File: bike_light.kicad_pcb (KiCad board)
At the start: 4 copper layers, 139.3 x 22.9 mm, 191 parts, among them P1 CONN_6_RA_MALE, P10 CONN_2, P11 CONN_2, P12 CONN_2, P13 CONN_2, P14 CONN_2, P15 CONN_2, P16 CONN_2, P2 CONN_2x2_MALE_RA, P3 CONN_2x2_MALE_RA, P4 CONN_2x2_FEMALE_BACK, P5 CONN_6_FEMALE_FRONT, P6 CONN_2x2_FEMALE_BACK, P7 CONN_2, P8 CONN_2, P9 CONN_2, Q1 AON7611, Q4 DMN65D8L, Q5 DMN65D8L, Q6 DMN65D8L, Q7 DMN65D8L, Q8 DMN65D8L, Q9 DMN65D8L, U1 TEST_PT, U10 TEST_PT, U11 TEST_PT, U12 TEST_PT, U13 TEST_PT, U14 TEST_PT, U15 TEST_PT, U16 TEST_PT, U17 TEST_PT, U18 TEST_PT, U19 TEST_PT, U2 TEST_PT, U20 MCP6L02, U21 74LVC2G06, U22 TPS3700, U23 NC7WZ08, U3 TEST_PT, U30 MSP430G2203IPW28, U31 BH1620FVC, U32 MMA7660FC, U33 AT42QT1011, U34 TOUCHPAD, U35 AT42QT1011, U36 TOUCHPAD, U37 AT42QT1011, U38 TOUCHPAD, U39 TLC59108IPWR, U4 TEST_PT, U40 TLC59108IPWR, U41 TLC59108IPWR, U42 TPS62090, U43 LM3668, U44 CONN_JTAG_14_2_wire, U45 CP2110, U46 ESDR0502N, U47 CONN_USB, U48 BQ24190, U5 TEST_PT, U6 TEST_PT, U7 TEST_PT, U8 TEST_PT, U9 TEST_PT

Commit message: finished other light module
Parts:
- moved R8 5.46 mm to (82.8, 91.2)
- moved C18 3.26 mm to (89.8, 91.2)
- moved R9 2.22 mm to (87.7, 91.2)
- moved C19 1.30 mm to (216.7, 87.9)
- moved C17 0.68 mm to (81.4, 88.5), turned to 270 degrees
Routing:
- net AGND: track 181.4 -> 222.4 mm, vias 30 -> 25
- net /output_signal_brake_2/signal_leds_front/CATHODE_8: track 0.00 -> 28.2 mm, vias 0 -> 2
- net /battery_charger/SCL: track 162.3 -> 182.3 mm, vias 4 -> 7
- net /battery_charger/SDA: track 173.5 -> 186.1 mm, vias 4 -> 6
- net /output_signal_brake_2/signal_leds_front/CATHODE_7: track 0.00 -> 10.9 mm
- net /output_signal_brake_2/signal_leds_front/CATHODE_5: track 0.00 -> 9.38 mm, vias 0 -> 1
- net +3.3V: track 125.8 -> 116.6 mm, vias 22 -> 24
- net /output_signal_brake_2/signal_leds_front/CATHODE_4: track 0.00 -> 8.21 mm, vias 0 -> 1
- net /output_signal_brake_2/signal_leds_front/CATHODE_6: track 0.00 -> 8.20 mm, vias 0 -> 1
- net /output_signal_brake_2/signal_leds_front/CATHODE_3: track 0.00 -> 7.54 mm, vias 0 -> 1
- net /output_signal_brake_2/brake_leds/CATHODE_7: track 5.28 -> 12.5 mm
- net /output_signal_brake_2/signal_leds_front/CATHODE_2: track 0.00 -> 7.01 mm, vias 0 -> 1
- net /output_signal_brake_2/brake_leds/CATHODE_8: track 22.2 -> 15.5 mm
- net /output_signal_brake_2/signal_leds_front/CATHODE_1: track 0.00 -> 6.03 mm, vias 0 -> 1
- net /output_signal_brake_2/signal_leds_back/CATHODE_8: track 21.0 -> 15.8 mm, vias 2 -> 3
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- added copper zone on B.Cu, net /output_signal_brake_2/signal_leds_front/CATHODE_8
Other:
- board size 139.3 x 22.9 mm -> 153.5 x 22.9 mm

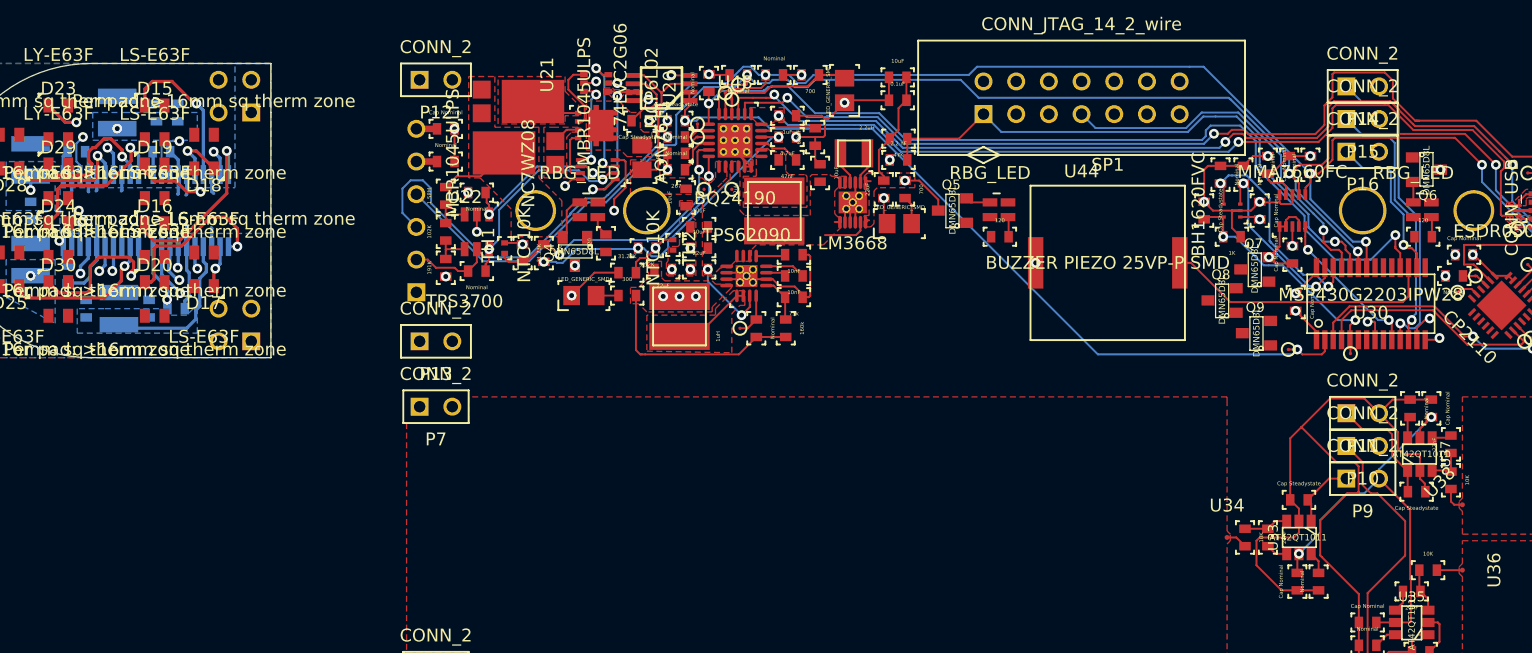
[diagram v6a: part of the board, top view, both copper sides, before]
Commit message: finished routing board, added vibrator module
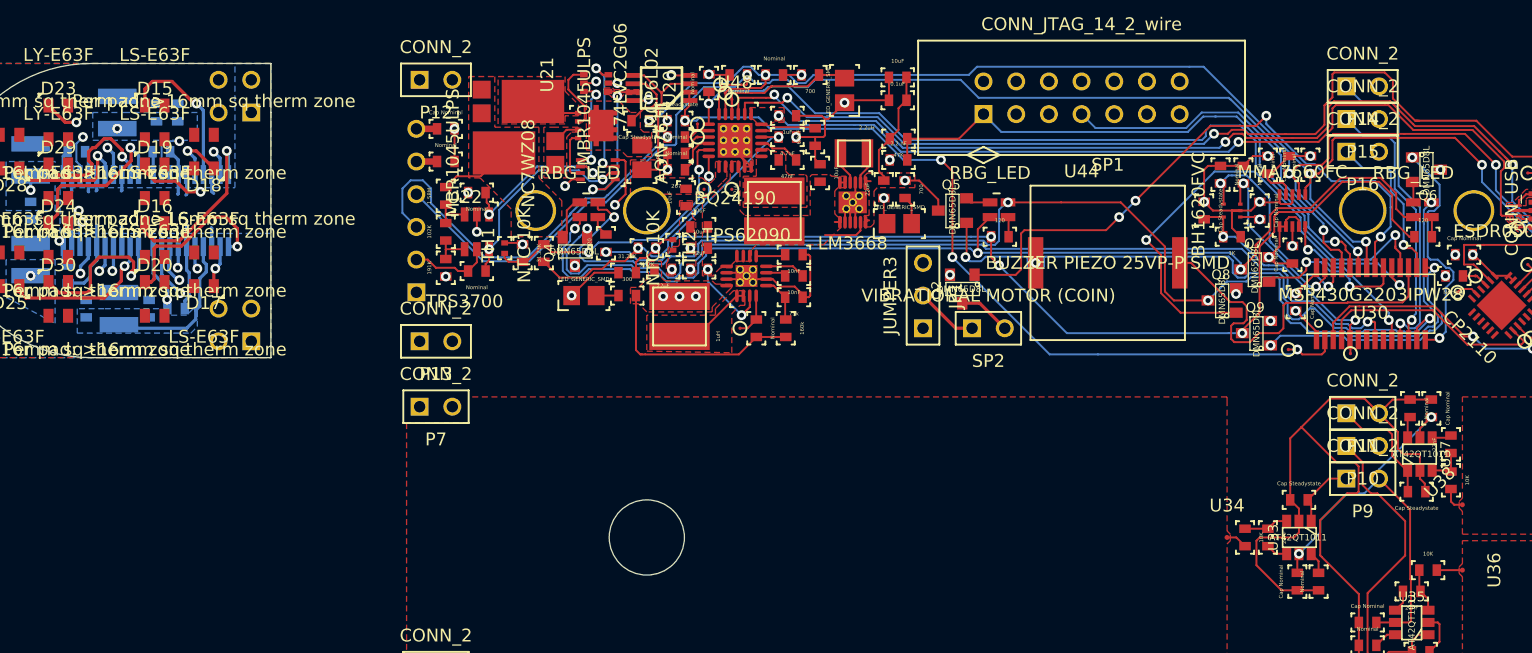
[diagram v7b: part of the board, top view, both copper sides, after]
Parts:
- added JP1: JUMPER3, CONN_3, F.Cu at (147.8, 92.7)
- added Q2: DMN65D8L, SOT23, F.Cu at (150.9, 89.7)
- added SP2: VIBRATIONAL MOTOR (COIN), CONN_2x1, F.Cu at (151.6, 92.7)
- moved U4 1.40 mm to (132.1, 73.8)
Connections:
- net /output_signal_brake_2/brake_leds/+2.5V renamed +2.5V
- U30 pad 21: (no net) -> /micro_proc/VIBRATOR
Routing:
- net N-0000093: track 0.00 -> 97.2 mm, vias 0 -> 4
- net N-0000092: track 0.00 -> 83.7 mm, vias 0 -> 3
- net N-0000097: track 0.00 -> 79.8 mm, vias 0 -> 4
- net /micro_proc/LED_1: track 1.94 -> 75.2 mm, vias 1 -> 2
- net /micro_proc/VIBRATOR: track 0.00 -> 48.1 mm, vias 0 -> 4
- net /micro_proc/LED_2: track 2.22 -> 49.1 mm, vias 1 -> 2
- net /output_general/GREEN_CTRL: track 0.00 -> 38.8 mm, vias 0 -> 2
- net /output_general/RED_CTRL: track 0.00 -> 20.0 mm, vias 0 -> 2
- net /micro_proc/LED_3: track 1.16 -> 18.4 mm, vias 1 -> 2
- net /output_general/BLUE_CTRL: track 0.00 -> 12.4 mm, vias 0 -> 2
- net /micro_proc/SPEAKER: track 21.4 -> 28.7 mm
- net N-0000094: track 0.00 -> 4.86 mm
- net N-0000095: track 0.00 -> 4.11 mm
- net /micro_proc/ADC_BATT: track 61.8 -> 65.7 mm, vias 2 -> 4
- net N-00000106: track 24.8 -> 25.8 mm, vias 3 -> 2
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- added copper zone on F.Cu, net N-00000173
- added copper zone on F.Cu, net N-00000195
- added copper zone on F.Cu, net N-0000079
- removed copper zone on F.Cu, net N-00000172
- removed copper zone on F.Cu, net N-00000196
- removed copper zone on F.Cu, net N-0000078
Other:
- board size 153.5 x 22.9 mm -> 153.5 x 39.8 mm
- board text added: "Front: Brake + Signal LED's Inner1: +3.3V Inner2: Routing Back: Driver IC's, fanout"

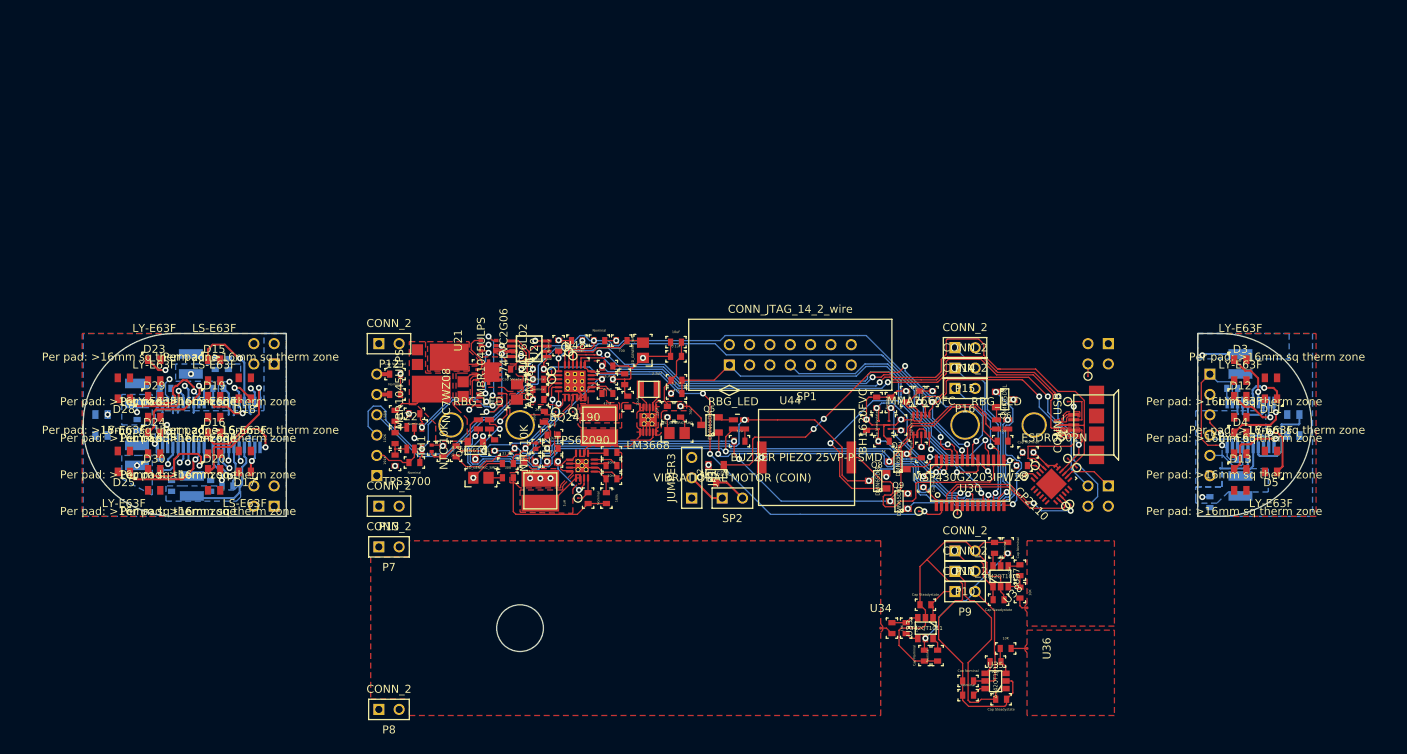
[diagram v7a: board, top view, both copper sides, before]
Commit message: revised board for manufacture
still need to panelize
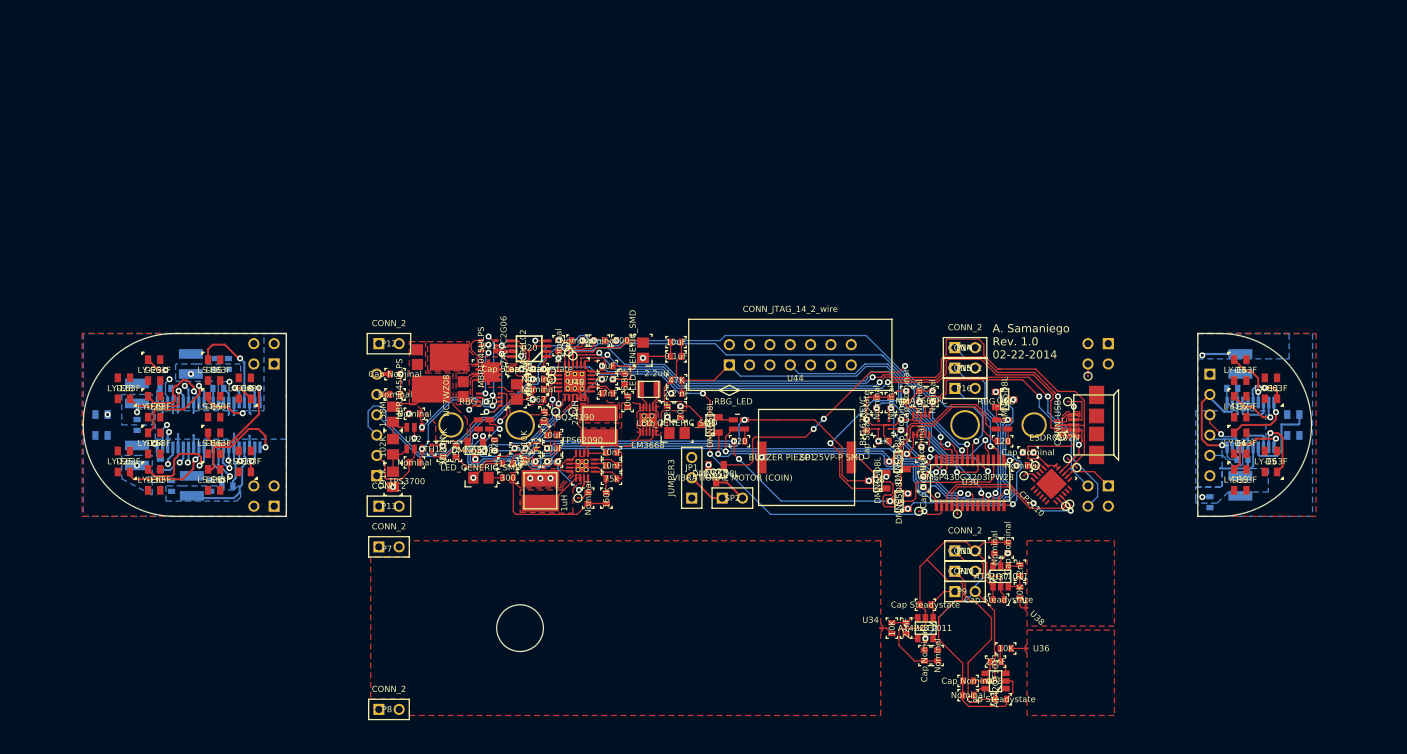
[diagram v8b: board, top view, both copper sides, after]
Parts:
- R2, R5, R6: footprint r_0603 -> r_0805
- U43: footprint WSON_12 -> WSON_12_thinpads
- moved R6 1.42 mm to (110.5, 89.4)
- moved R2 1.17 mm to (110.5, 81.3)
- moved R5 0.28 mm to (110.5, 85.3)
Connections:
- P1 pad 1: +3.3V -> +2.5V
- P1 pad 2: +2.5V -> +3.3V
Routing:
- net N-00000192: track 2.95 -> 4.16 mm
- net N-00000191: track 2.95 -> 4.16 mm
- added copper zone on F.Cu, net N-00000160
- added copper zone on F.Cu, net N-00000196
- removed copper zone on F.Cu, net N-00000173
- removed copper zone on F.Cu, net N-00000195
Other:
- rule pad_to_mask_clearance: 0 -> 0.1778
- board text added: "A. Samaniego Rev. 1.0 02-22-2014"
